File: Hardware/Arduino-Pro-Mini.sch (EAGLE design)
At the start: 30 parts, among them Q1 8/16/20MHz, U1 ATMEGA328, U2 MIC5205

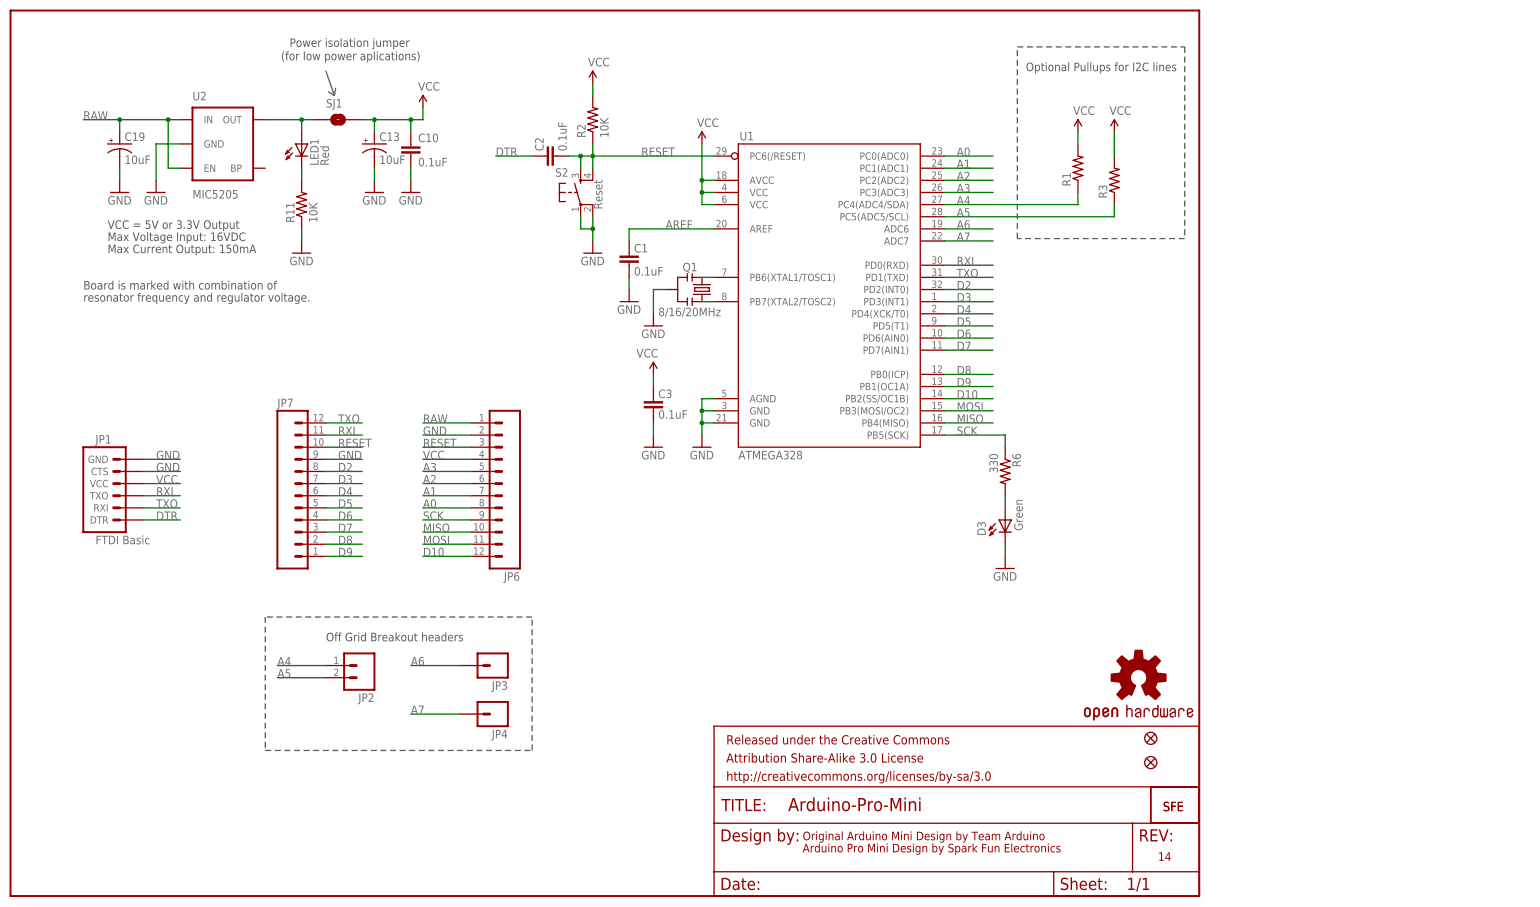
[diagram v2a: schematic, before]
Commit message: footprint updates, schematic work
-reset button, moved pads out for more toe
-resonator, 1:1 with fake traces
-moved all labels to flags in sch
-moved A6/A7 header to 2X1, rather than singles
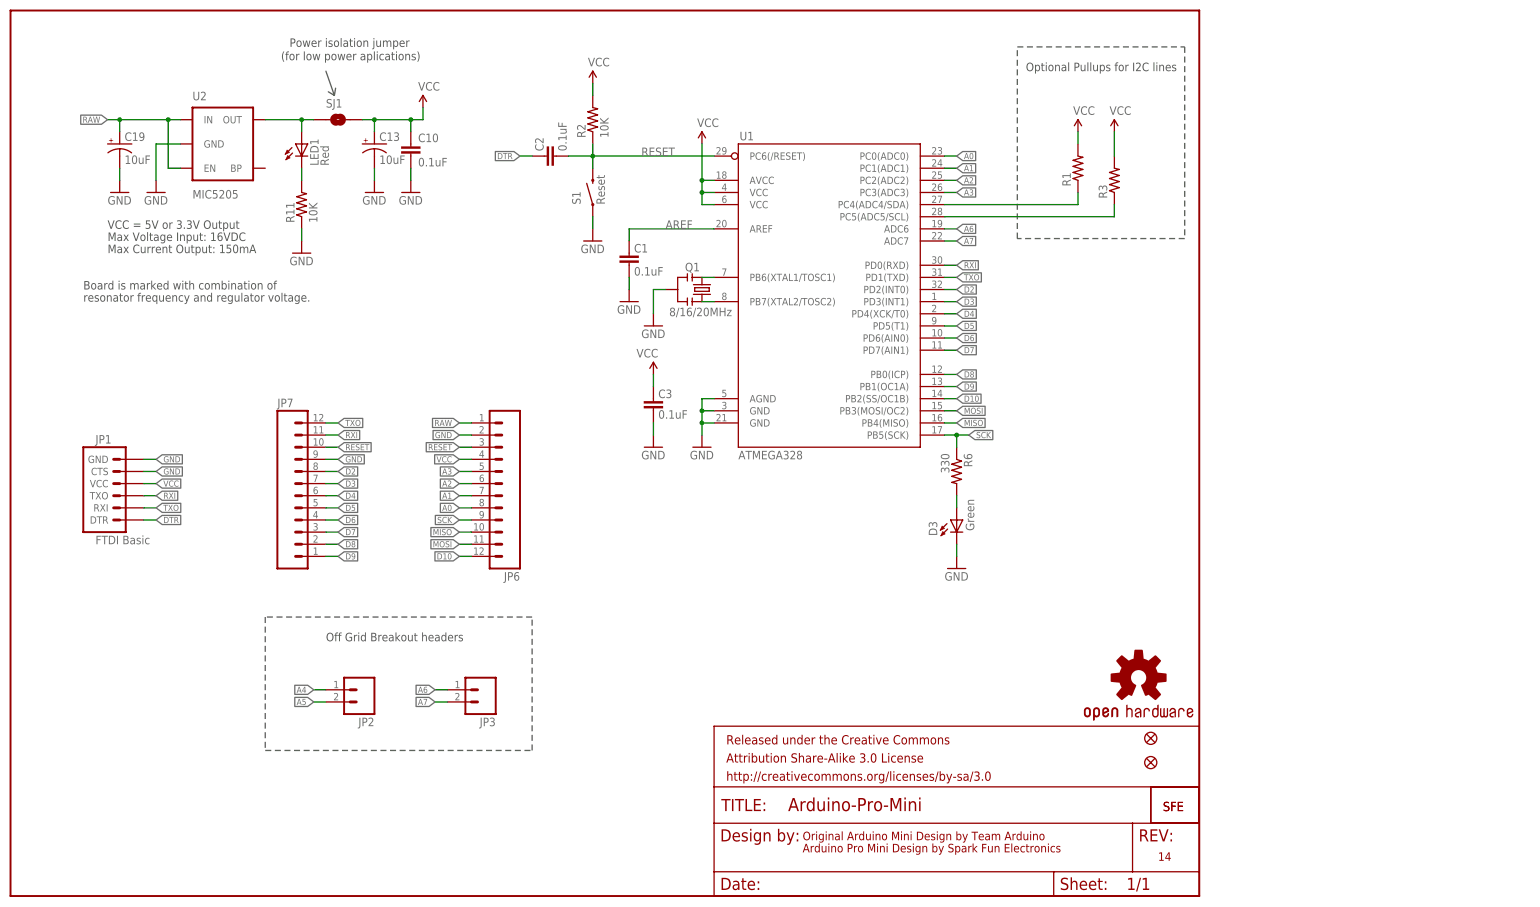
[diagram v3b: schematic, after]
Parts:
- removed JP4: M01PTH, SparkFun:M01PTH
- removed S2: Reset, SparkFun:TAC_SWITCHSMD
- added S1: Reset, Testing:SWITCH-MOMENTARY-2SMD-ALT01
- JP3: value M01PTH -> (none); device SparkFun:M01PTH -> SparkFun:M02PTH
- Q1: device SparkFun:RESONATORSMD -> Testing:RESONATOR1:1
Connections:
- net A7: now also JP3.2; no longer JP4.1
- net GND: now also S1.1; no longer S2.1, S2.2
- net N$1: now also Q1.3; no longer Q1.1
- net N$2: now also Q1.1; no longer Q1.3
- net RESET: now also S1.2; no longer S2.3, S2.4
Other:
- moved on the sheet: D3, JP2, Q1, R6

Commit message: v14 ready for protos
changed led footprint to cloaser to true 0603
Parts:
- D3, LED1: device SparkFun:LED0603 -> Testing:LED
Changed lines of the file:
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@@
 <grid distance="0.1" unitdist="inch" unit="inch" style="lines" multiple="1" display="no" altdistance="0.01" altunitdist="inch" altunit="inch"/>
 <layers>
-<layer number="1" name="Top" color="4" fill="1" visible="no" active="no"/>
-<layer number="2" name="Route2" color="1" fill="3" visible="no" active="no"/>
-<layer number="3" name="Route3" color="4" fill="3" visible="no" active="no"/>
-<layer number="4" name="Route4" color="1" fill="4" visible="no" active="no"/>
-<layer number="5" name="Route5" color="4" fill="4" visible="no" active="no"/>
-<layer number="6" name="Route6" color="1" fill="8" visible="no" active="no"/>
-<layer number="7" name="Route7" color="4" fill="8" visible="no" active="no"/>
-<layer number="8" name="Route8" color="1" fill="2" visible="no" active="no"/>
-<layer number="9" name="Route9" color="4" fill="2" visible="no" active="no"/>
-<layer number="10" name="Route10" color="1" fill="7" visible="no" active="no"/>
-<layer number="11" name="Route11" color="4" fill="7" visible="no" active="no"/>
-<layer number="12" name="Route12" color="1" fill="5" visible="no" active="no"/>
-<layer number="13" name="Route13" color="4" fill="5" visible="no" active="no"/>
-<layer number="14" name="Route14" color="1" fill="6" visible="no" active="no"/>
-<layer number="15" name="Route15" color="4" fill="6" visible="no" active="no"/>
-<layer number="16" name="Bottom" color="1" fill="1" visible="no" active="no"/>
-<layer number="17" name="Pads" color="2" fill="1" visible="no" active="no"/>
-<layer number="18" name="Vias" color="2" fill="1" visible="no" active="no"/>
-<layer number="19" name="Unrouted" color="6" fill="1" visible="no" active="no"/>
-<layer number="20" name="Dimension" color="6" fill="1" visible="no" active="no"/>
-<layer number="21" name="tPlace" color="16" fill="1" visible="no" active="no"/>
-<layer number="22" name="bPlace" color="14" fill="1" visible="no" active="no"/>
-<layer number="23" name="tOrigins" color="15" fill="1" visible="no" active="no"/>
-<layer number="24" name="bOrigins" color="15" fill="1" visible="no" active="no"/>
-<layer number="25" name="tNames" color="7" fill="1" visible="no" active="no"/>
-<layer number="26" name="bNames" color="7" fill="1" visible="no" active="no"/>
-<layer number="27" name="tValues" color="7" fill="1" visible="no" active="no"/>
-<layer number="28" name="bValues" color="7" fill="1" visible="no" active="no"/>
+<layer number="1" name="Top" color="4" fill="1" visible="yes" active="no"/>
+<layer number="2" name="Route2" color="1" fill="3" visible="yes" active="no"/>
+<layer number="3" name="Route3" color="4" fill="3" visible="yes" active="no"/>
+<layer number="4" name="Route4" color="1" fill="4" visible="yes" active="no"/>
+<layer number="5" name="Route5" color="4" fill="4" visible="yes" active="no"/>
+<layer number="6" name="Route6" color="1" fill="8" visible="yes" active="no"/>
+<layer number="7" name="Route7" color="4" fill="8" visible="yes" active="no"/>
+<layer number="8" name="Route8" color="1" fill="2" visible="yes" active="no"/>
+<layer number="9" name="Route9" color="4" fill="2" visible="yes" active="no"/>
+<layer number="10" name="Route10" color="1" fill="7" visible="yes" active="no"/>
+<layer number="11" name="Route11" color="4" fill="7" visible="yes" active="no"/>
+<layer number="12" name="Route12" color="1" fill="5" visible="yes" active="no"/>
+<layer number="13" name="Route13" color="4" fill="5" visible="yes" active="no"/>
+<layer number="14" name="Route14" color="1" fill="6" visible="yes" active="no"/>
+<layer number="15" name="Route15" color="4" fill="6" visible="yes" active="no"/>
+<layer number="16" name="Bottom" color="1" fill="1" visible="yes" active="no"/>
+<layer number="17" name="Pads" color="2" fill="1" visible="yes" active="no"/>
+<layer number="18" name="Vias" color="2" fill="1" visible="yes" active="no"/>
+<layer number="19" name="Unrouted" color="6" fill="1" visible="yes" active="no"/>
+<layer number="20" name="Dimension" color="6" fill="1" visible="yes" active="no"/>
+<layer number="21" name="tPlace" color="16" fill="1" visible="yes" active="no"/>
+<layer number="22" name="bPlace" color="14" fill="1" visible="yes" active="no"/>
+<layer number="23" name="tOrigins" color="15" fill="1" visible="yes" active="no"/>
+<layer number="24" name="bOrigins" color="15" fill="1" visible="yes" active="no"/>
+<layer number="25" name="tNames" color="7" fill="1" visible="yes" active="no"/>
+<layer number="26" name="bNames" color="7" fill="1" visible="yes" active="no"/>
+<layer number="27" name="tValues" color="7" fill="1" visible="yes" active="no"/>
+<layer number="28" name="bValues" color="7" fill="1" visible="yes" active="no"/>
 <layer number="29" name="tStop" color="7" fill="3" visible="no" active="no"/>
 <layer number="30" name="bStop" color="7" fill="6" visible="no" active="no"/>
@@
 <layer number="35" name="tGlue" color="7" fill="4" visible="no" active="no"/>
 <layer number="36" name="bGlue" color="7" fill="5" visible="no" active="no"/>
-<layer number="37" name="tTest" color="7" fill="1" visible="no" active="no"/>
-<layer number="38" name="bTest" color="7" fill="1" visible="no" active="no"/>
+<layer number="37" name="tTest" color="7" fill="1" visible="yes" active="no"/>
+<layer number="38" name="bTest" color="7" fill="1" visible="yes" active="no"/>
 <layer number="39" name="tKeepout" color="4" fill="11" visible="no" active="no"/>
 <layer number="40" name="bKeepout" color="1" fill="11" visible="no" active="no"/>
@@
 <layer number="44" name="Drills" color="7" fill="1" visible="no" active="no"/>
 <layer number="45" name="Holes" color="7" fill="1" visible="no" active="no"/>
-<layer number="46" name="Milling" color="3" fill="1" visible="no" active="no"/>
-<layer number="47" name="Measures" color="7" fill="1" visible="no" active="no"/>
-<layer number="48" name="Document" color="7" fill="1" visible="no" active="no"/>
-<layer number="49" name="Reference" color="7" fill="1" visible="no" active="no"/>
-<layer number="50" name="dxf" color="7" fill="1" visible="no" active="no"/>
-<layer number="51" name="tDocu" color="6" fill="1" visible="no" active="no"/>
-<layer number="52" name="bDocu" color="7" fill="1" visible="no" active="no"/>
-<layer number="53" name="tGND_GNDA" color="7" fill="9" visible="no" active="no"/>
-<layer number="54" name="bGND_GNDA" color="1" fill="9" visible="no" active="no"/>
-<layer number="56" name="wert" color="7" fill="1" visible="no" active="no"/>
+<layer number="46" name="Milling" color="3" fill="1" visible="yes" active="no"/>
+<layer number="47" name="Measures" color="7" fill="1" visible="yes" active="no"/>
+<layer number="48" name="Document" color="7" fill="1" visible="yes" active="no"/>
+<layer number="49" name="Reference" color="7" fill="1" visible="yes" active="no"/>
+<layer number="50" name="dxf" color="7" fill="1" visible="yes" active="no"/>
+<layer number="51" name="tDocu" color="6" fill="1" visible="yes" active="no"/>
+<layer number="52" name="bDocu" color="7" fill="1" visible="yes" active="no"/>
+<layer number="53" name="tGND_GNDA" color="7" fill="9" visible="yes" active="no"/>
+<layer number="54" name="bGND_GNDA" color="1" fill="9" visible="yes" active="no"/>
+<layer number="56" name="wert" color="7" fill="1" visible="yes" active="no"/>
 <layer number="91" name="Nets" color="2" fill="1" visible="yes" active="yes"/>
 <layer number="92" name="Busses" color="1" fill="1" visible="yes" active="yes"/>
@@
 <part name="GND26" library="SparkFun" deviceset="GND" device=""/>
 <part name="R11" library="SparkFun" deviceset="RESISTOR" device="0603-RES" value="10K"/>
-<part name="LED1" library="SparkFun" deviceset="LED" device="0603" value="Red"/>
+<part name="LED1" library="Testing" deviceset="LED" device="" value="Red"/>
 <part name="GND28" library="SparkFun" deviceset="GND" device=""/>
 <part name="R2" library="SparkFun" deviceset="RESISTOR" device="0603-RES" value="10K"/>
@@
 <part name="GND7" library="SparkFun" deviceset="GND" device=""/>
 <part name="R6" library="SparkFun" deviceset="RESISTOR" device="0603-RES" value="330"/>
-<part name="D3" library="SparkFun" deviceset="LED" device="0603" value="Green"/>
+<part name="D3" library="Testing" deviceset="LED" device="" value="Green"/>
 <part name="GND8" library="SparkFun" deviceset="GND" device=""/>
 <part name="U$11" library="SparkFun" deviceset="LOGO-SFE" device="NEW"/>

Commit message: Finished design review and checklist
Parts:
- removed U$1: LOGO-SFESK, SparkFun:LOGO-SFESK
- removed U$11: LOGO-SFENEW, SparkFun:LOGO-SFENEW
- removed U$3: OSHW-LOGOS, SparkFun:OSHW-LOGOS
- Q1: device Testing:RESONATOR1:1 -> SparkFun:RESONATOR1:1
- renumbered FRAME1 to FRAME2
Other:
- note added: "15"
- note added: "Revised by: Marshall Taylor"
- note removed: "14"
- moved on the sheet: R2

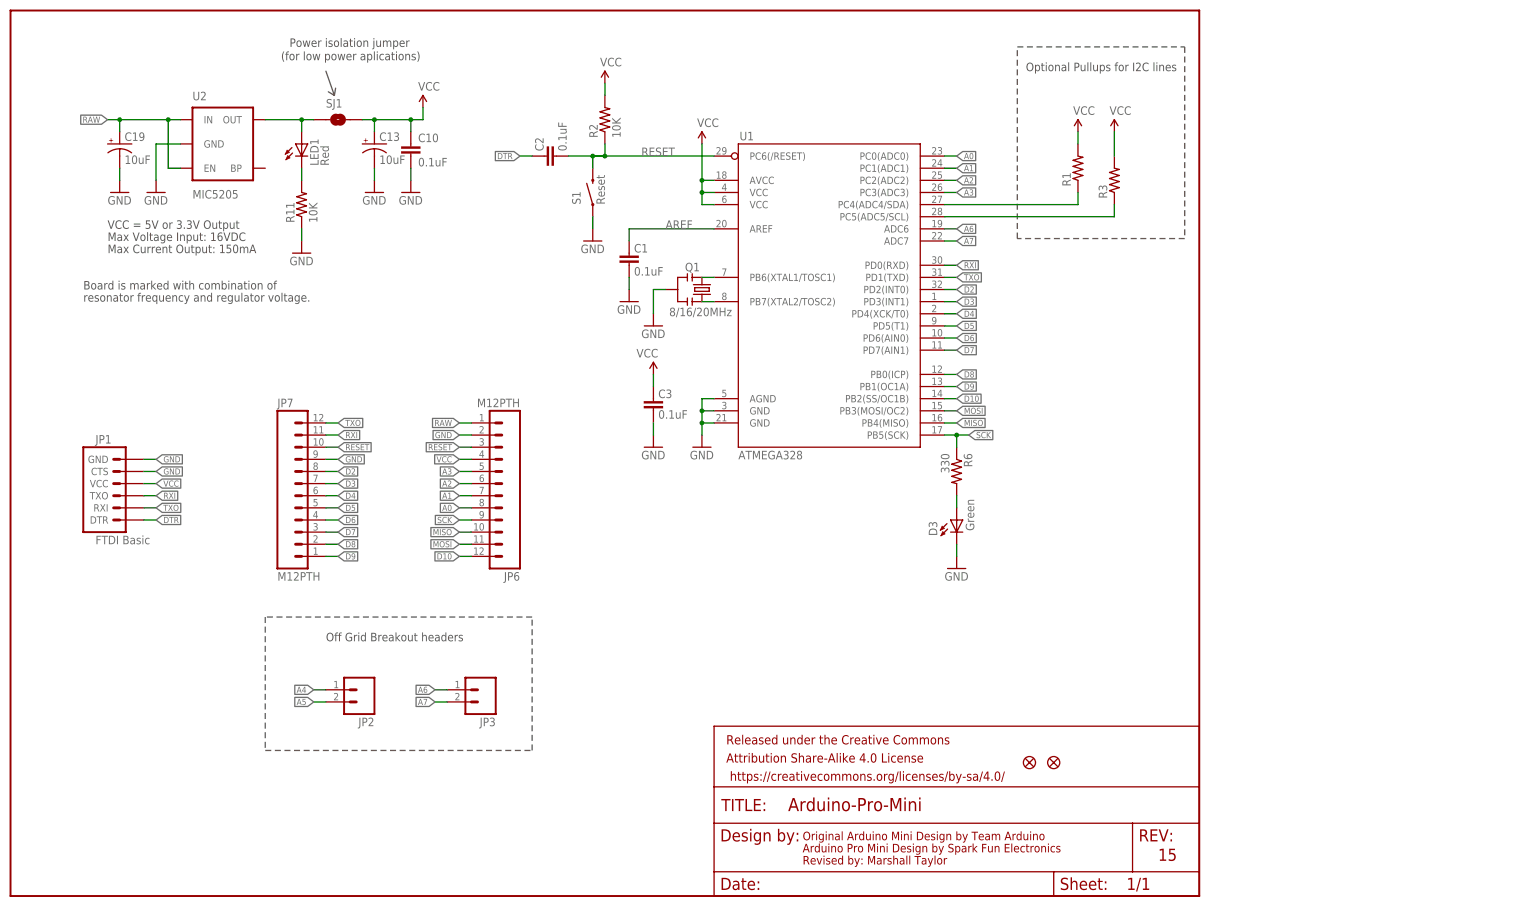
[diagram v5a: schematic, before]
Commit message: Updated schematic to standard
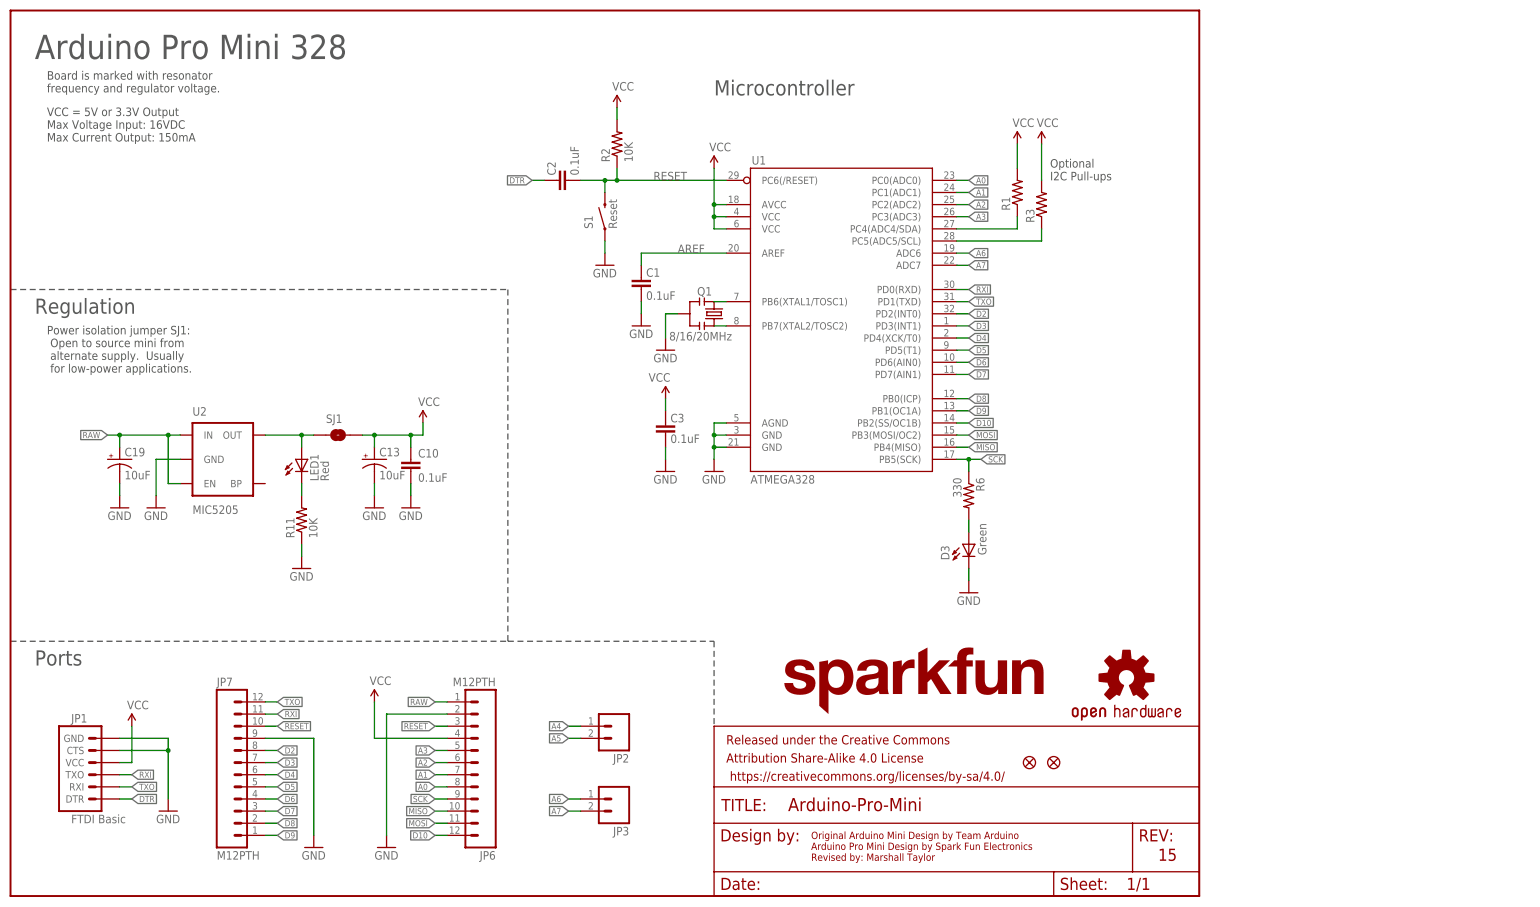
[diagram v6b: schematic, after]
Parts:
- C1, C10, C2, C3: PROD_ID (none) -> CAP-00810
- C13, C19: PROD_ID (none) -> CAP-00811
- D3: PROD_ID (none) -> DIO-00821
- LED1: PROD_ID (none) -> DIO-00819
- Q1: PROD_ID (none) -> XTAL-08900
- R11, R2: PROD_ID (none) -> RES-00824
- R6: PROD_ID (none) -> RES-00818
- S1: PROD_ID (none) -> SWCH-08247
- U1: PROD_ID (none) -> IC-09069
- U2: PROD_ID (none) -> VREG-00823
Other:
- note added: "Arduino Pro Mini 328"
- note added: "Board is marked with resonator frequency and regulator voltage."
- note added: "Microcontroller"
- note added: "Optional I2C Pull-ups"
- note added: "Original Arduino Mini Design by Team Arduino Arduino Pro Mini Design by Spark Fun Electronics Revised by: Marshall Taylor"
- note added: "Ports"
- note added: "Power isolation jumper SJ1: Open to source mini from alternate supply. Usually for low-power applications."
- note added: "Regulation"
- note added: "VCC = 5V or 3.3V Output Max Voltage Input: 16VDC Max Current Output: 150mA"
- note removed: "(for low power aplications)"
- note removed: "Arduino Pro Mini Design by Spark Fun Electronics"
- note removed: "Board is marked with combination of"
- note removed: "Max Current Output: 150mA"
- note removed: "Max Voltage Input: 16VDC"
- note removed: "Off Grid Breakout headers"
- note removed: "Optional Pullups for I2C lines"
- note removed: "Original Arduino Mini Design by Team Arduino"
- note removed: "Power isolation jumper"
- note removed: "Revised by: Marshall Taylor"
- note removed: "VCC = 5V or 3.3V Output"
- note removed: "resonator frequency and regulator voltage."
- moved on the sheet: C1, C10, C13, C19, C2, C3, D3, JP1, JP2, JP3, JP6, JP7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
